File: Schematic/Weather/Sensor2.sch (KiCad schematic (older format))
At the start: 0 parts

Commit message: more changes
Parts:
- added J8: 4_Way_Wire, Connector_PinHeader_2.54mm:PinHeader_1x04_P2.54mm_Vertical, symbol MyComponents:4_Way_Wire
- added MOD2: HTU21, footprint:HTU21, symbol MyComponents:HTU21
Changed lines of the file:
@@
 $Descr A4 11693 8268
 encoding utf-8
-Sheet 9 14
+Sheet 8 15
 Title ""
 Date ""
@@
 Comment4 ""
 $EndDescr
-Text HLabel 2500 1500 0    50   Input ~ 0
+Text HLabel 2850 2800 0    50   Input ~ 0
 J12_P1
-Text HLabel 2500 1700 0    50   Input ~ 0
+Text HLabel 2850 3000 0    50   Input ~ 0
 J12_P2
-Text HLabel 2500 1900 0    50   Input ~ 0
+Text HLabel 2850 3200 0    50   Input ~ 0
 J12_P3
-Text HLabel 2500 2100 0    50   Input ~ 0
+Text HLabel 2850 3400 0    50   Input ~ 0
 J12_P4
+$Comp
+L MyComponents:HTU21 MOD2
+U 1 1 5CB467F0
+P 7400 2900
+F 0 "MOD2" H 8028 2896 50  0000 L CNN
+F 1 "HTU21" H 8028 2805 50  0000 L CNN
+F 2 "footprint:HTU21" H 7600 2600 50  0001 C CNN
+F 3 "" H 7600 2600 50  0001 C CNN
+	1    7400 2900
+	1    0    0    -1
+$EndComp
+$Comp
+L MyComponents:4_Way_Wire J8
+U 1 1 5CB4EF7C
+P 5700 2700
+F 0 "J8" H 5869 2461 50  0000 L CNN
+F 1 "4_Way_Wire" H 5869 2370 50  0000 L CNN
+F 2 "Connector_PinHeader_2.54mm:PinHeader_1x04_P2.54mm_Vertical" H 5600 2750 50  0001 C CNN
+F 3 "" H 5600 2750 50  0001 C CNN
+	1    5700 2700
+	1    0    0    -1
+$EndComp
 $EndSCHEMATC

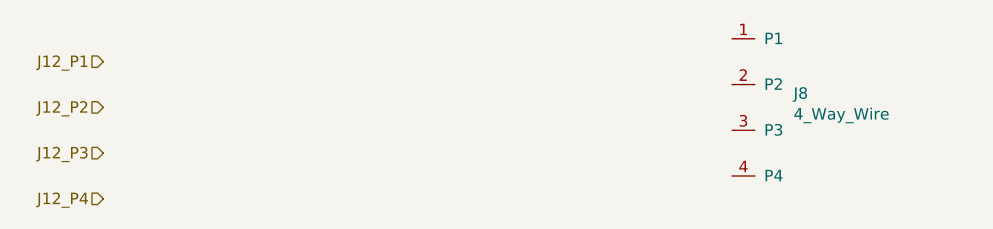
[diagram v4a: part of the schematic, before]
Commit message: Connector relable start
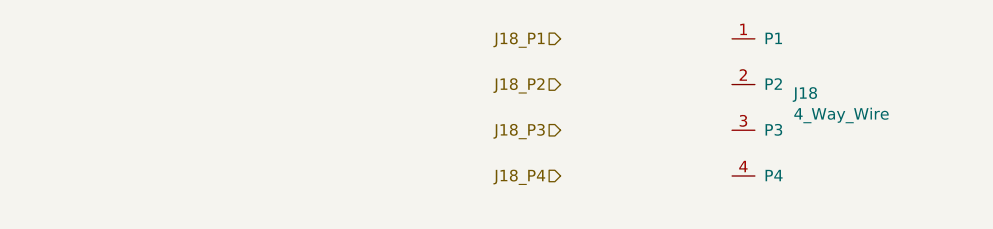
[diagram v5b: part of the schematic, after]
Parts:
- renumbered J8 to J18
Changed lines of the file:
@@
 $Descr A4 11693 8268
 encoding utf-8
-Sheet 8 15
+Sheet 14 15
 Title ""
 Date ""
@@
 Comment4 ""
 $EndDescr
-Text HLabel 2850 2800 0    50   Input ~ 0
-J12_P1
-Text HLabel 2850 3000 0    50   Input ~ 0
-J12_P2
-Text HLabel 2850 3200 0    50   Input ~ 0
-J12_P3
-Text HLabel 2850 3400 0    50   Input ~ 0
-J12_P4
+Text HLabel 4850 2700 0    50   Input ~ 0
+J18_P1
+Text HLabel 4850 2900 0    50   Input ~ 0
+J18_P2
+Text HLabel 4850 3100 0    50   Input ~ 0
+J18_P3
+Text HLabel 4850 3300 0    50   Input ~ 0
+J18_P4
 $Comp
 L MyComponents:HTU21 MOD2
@@
 $EndComp
 $Comp
-L MyComponents:4_Way_Wire J8
+L MyComponents:4_Way_Wire J18
 U 1 1 5CB4EF7C
 P 5700 2700
-F 0 "J8" H 5869 2461 50  0000 L CNN
+F 0 "J18" H 5869 2461 50  0000 L CNN
 F 1 "4_Way_Wire" H 5869 2370 50  0000 L CNN
 F 2 "Connector_PinHeader_2.54mm:PinHeader_1x04_P2.54mm_Vertical" H 5600 2750 50  0001 C CNN

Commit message: schm update
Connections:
- net J18_P1: now also J18.1 (P1), MOD2.1 (VCC)
- net J18_P2: now also J18.2 (P2), MOD2.2 (GND)
- net J18_P3: now also J18.3 (P3), MOD2.3 (SCL)
- net J18_P4: now also J18.4 (P4), MOD2.4 (SDA)
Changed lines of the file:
@@
 L MyComponents:HTU21 MOD2
 U 1 1 5CB467F0
-P 7400 2900
-F 0 "MOD2" H 8028 2896 50  0000 L CNN
-F 1 "HTU21" H 8028 2805 50  0000 L CNN
-F 2 "footprint:HTU21" H 7600 2600 50  0001 C CNN
-F 3 "" H 7600 2600 50  0001 C CNN
-	1    7400 2900
-	1    0    0    -1
+P 7400 3150
+F 0 "MOD2" H 8028 3146 50  0000 L CNN
+F 1 "HTU21" H 8028 3055 50  0000 L CNN
+F 2 "footprint:HTU21" H 7600 2850 50  0001 C CNN
+F 3 "" H 7600 2850 50  0001 C CNN
+	1    7400 3150
+	1    0    0    1
 $EndComp
 $Comp
@@
 U 1 1 5CB4EF7C
 P 5700 2700
-F 0 "J18" H 5869 2461 50  0000 L CNN
-F 1 "4_Way_Wire" H 5869 2370 50  0000 L CNN
+F 0 "J18" H 5700 2850 50  0000 L CNN
+F 1 "4_Way_Wire" H 5700 2000 50  0000 L CNN
 F 2 "Connector_PinHeader_2.54mm:PinHeader_1x04_P2.54mm_Vertical" H 5600 2750 50  0001 C CNN
 F 3 "" H 5600 2750 50  0001 C CNN
@@
 	1    0    0    -1
 $EndComp
+Wire Wire Line
+	4850 2700 5600 2700
+Wire Wire Line
+	4850 2900 5600 2900
+Wire Wire Line
+	4850 3100 5600 3100
+Wire Wire Line
+	4850 3300 5600 3300
+Wire Wire Line
+	7300 3250 7000 3250
+Wire Wire Line
+	7000 3250 7000 3500
+Wire Wire Line
+	7000 3500 5600 3500
+Wire Wire Line
+	5600 3500 5600 3300
+Connection ~ 5600 3300
+Wire Wire Line
+	7300 2800 7000 2800
+Wire Wire Line
+	7000 2800 7000 2500
+Wire Wire Line
+	7000 2500 5600 2500
+Wire Wire Line
+	5600 2500 5600 2700
+Connection ~ 5600 2700
+Wire Wire Line
+	7300 2950 6750 2950
+Wire Wire Line
+	6750 2950 6750 2800
+Wire Wire Line
+	6750 2800 5600 2800
+Wire Wire Line
+	5600 2800 5600 2900
+Connection ~ 5600 2900
+Wire Wire Line
+	7300 3100 6750 3100
+Wire Wire Line
+	6750 3100 6750 3200
+Wire Wire Line
+	6750 3200 5600 3200
+Wire Wire Line
+	5600 3200 5600 3100
+Connection ~ 5600 3100
 $EndSCHEMATC
